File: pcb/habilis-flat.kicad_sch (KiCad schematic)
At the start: 74 parts, among them SW1 MX, SW10 MX, SW11 MX, SW12 MX, SW13 MX, SW14 MX, SW15 MX, SW16 MX, SW17 MX, SW18 MX, SW19 MX, SW2 MX, SW20 MX, SW21 MX, SW22 MX, SW23 MX, SW24 MX, SW25 MX, SW26 MX, SW27 MX, SW28 MX, SW29 MX, SW3 MX, SW30 MX, SW31 MX, SW32 MX, SW33 MX, SW34 MX, SW35 MX, SW4 MX, SW5 MX, SW6 MX, SW7 MX, SW8 MX, SW9 MX, U1 ProMicro

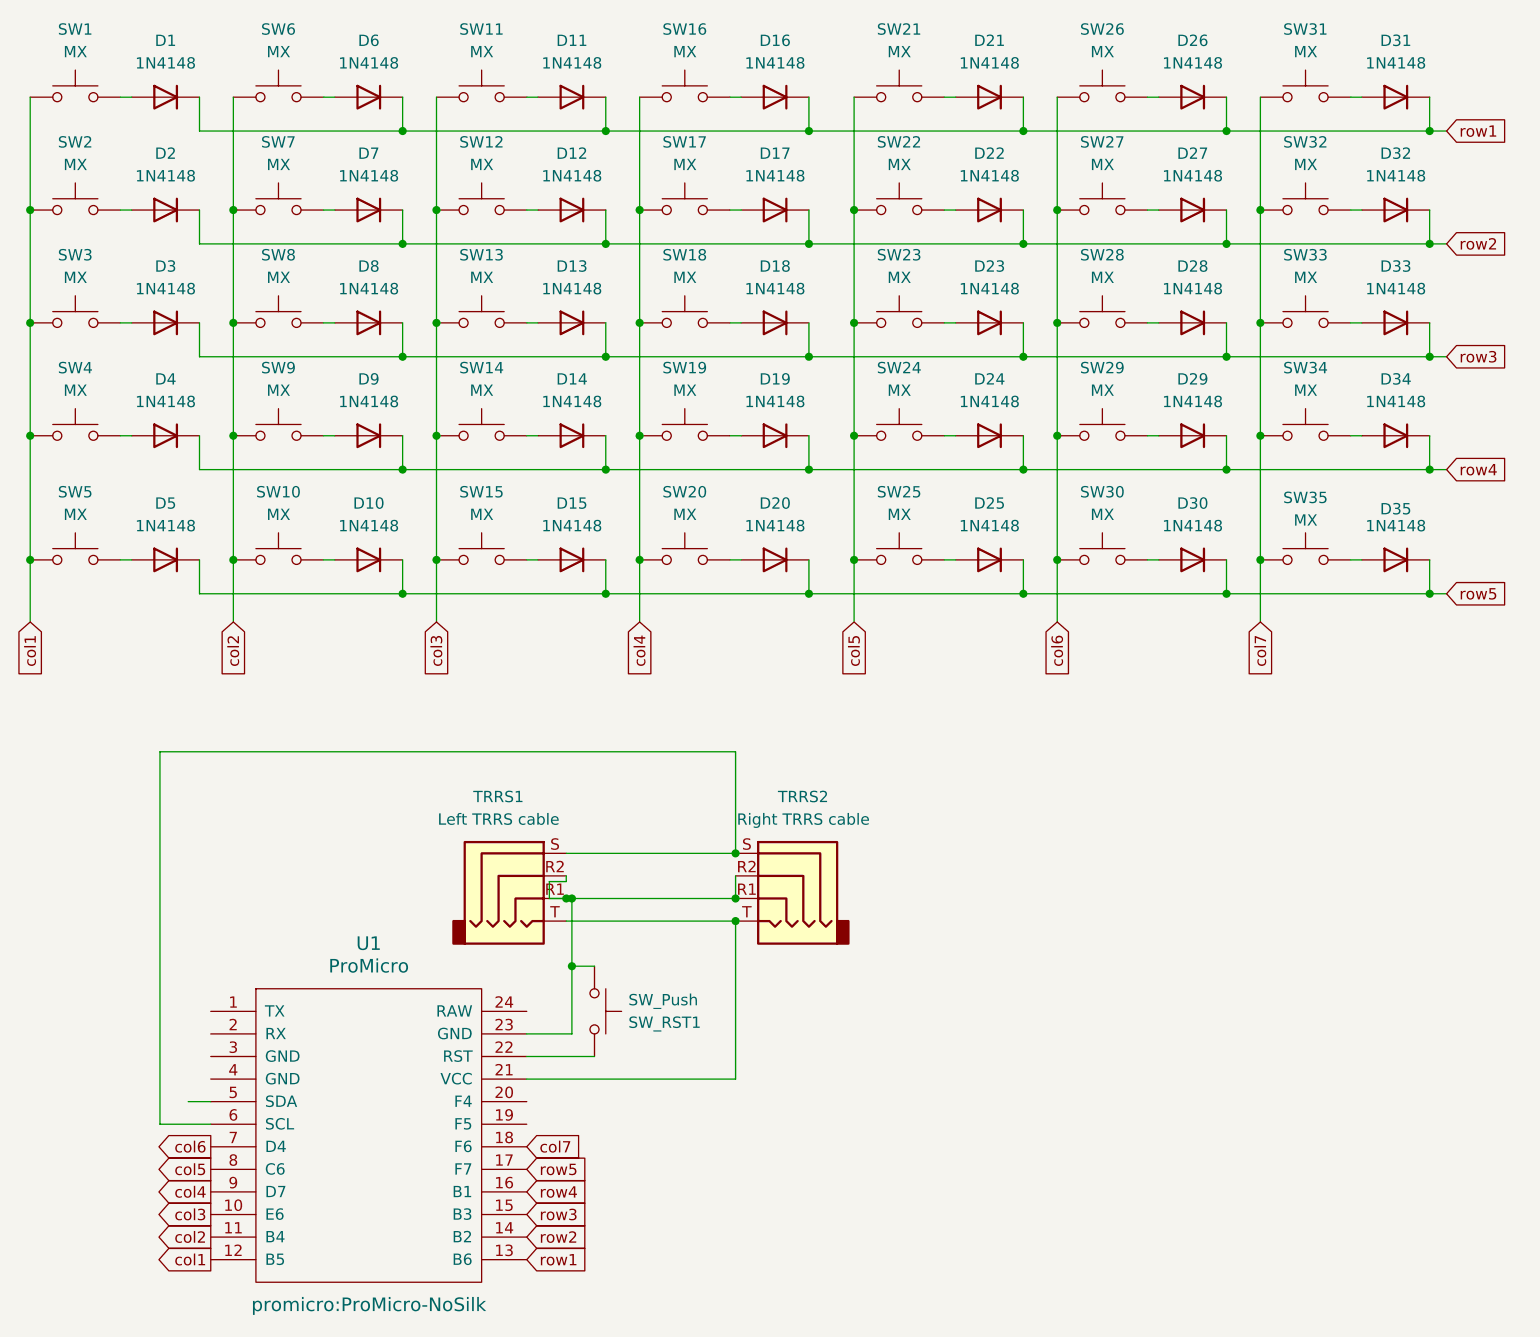
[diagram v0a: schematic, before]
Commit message: Renumber rows and columns to start at 0
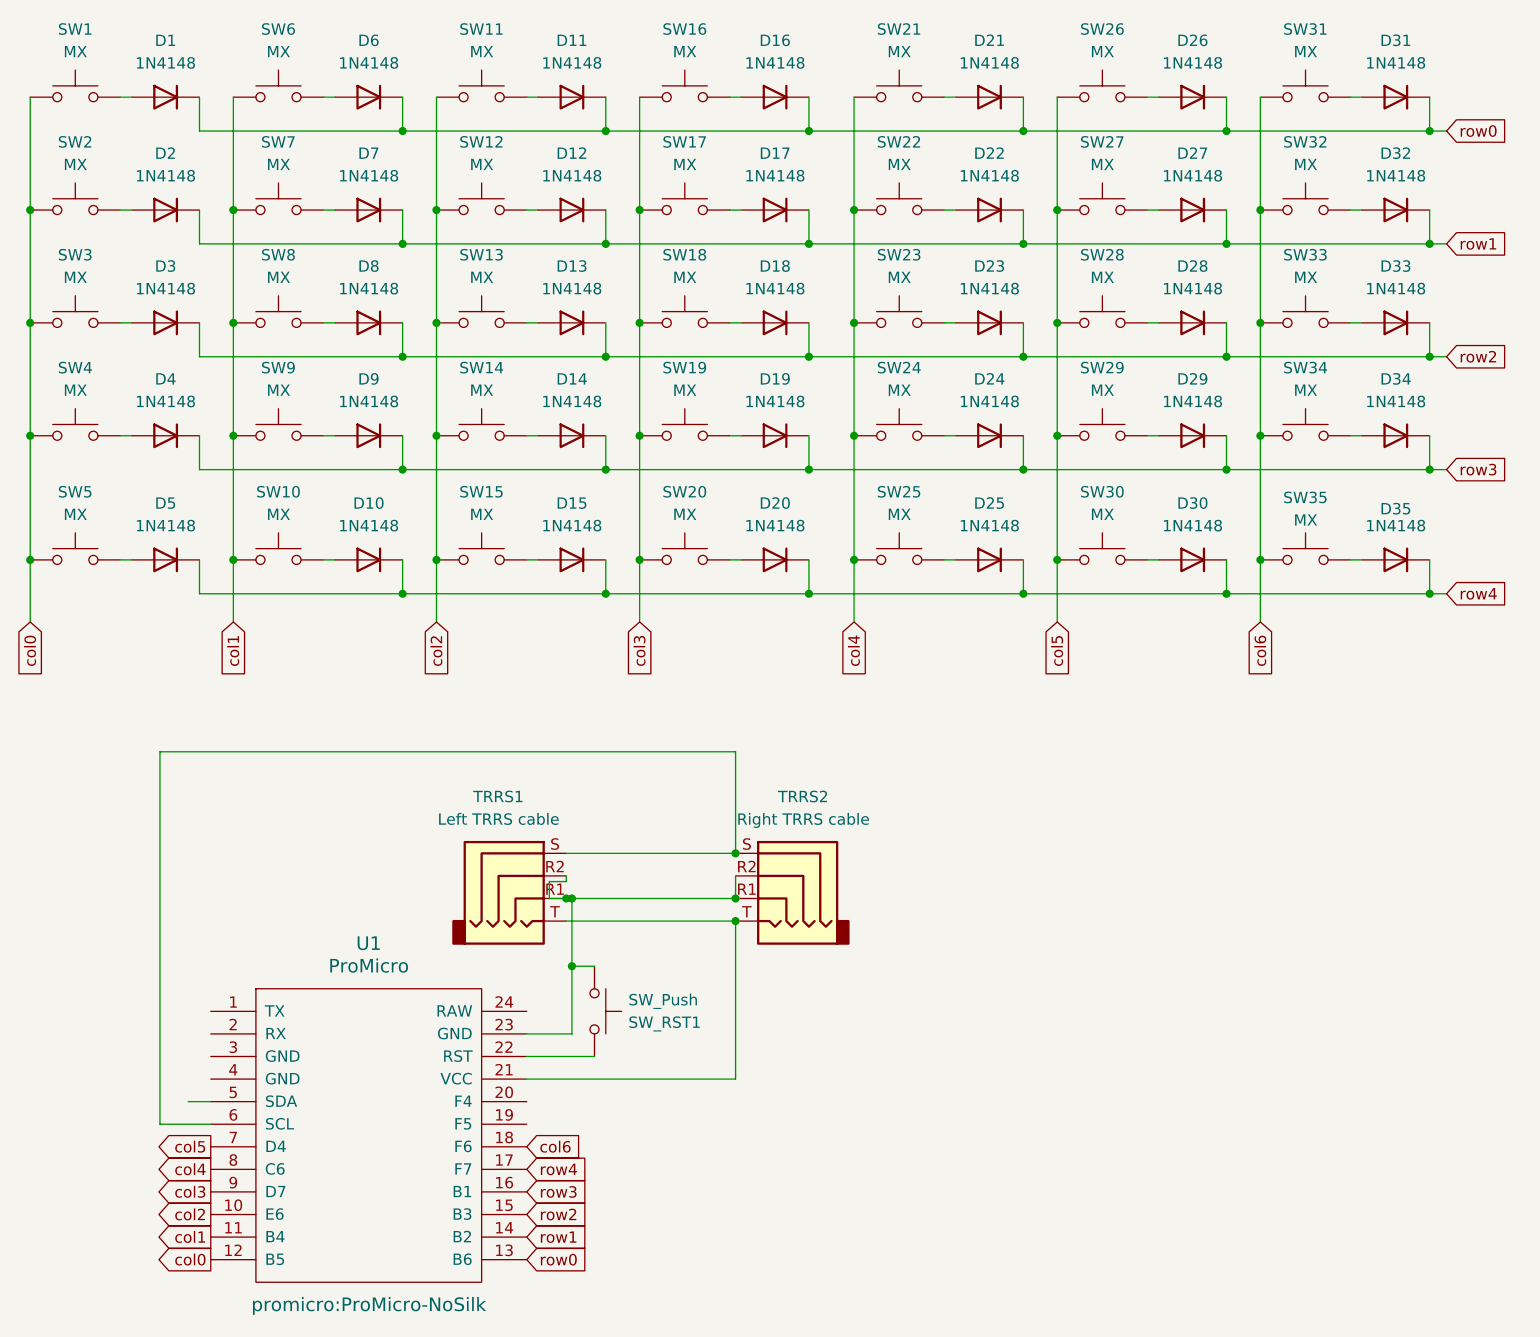
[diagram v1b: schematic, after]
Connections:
- net col7 is gone; now on net col6: SW31.2, SW32.2, SW33.1, SW34.2, SW35.2, U1.18 (F6)
- net row5 is gone; now on net row4: D10.1 (K), D15.1 (K), D20.1 (K), D25.1 (K), D30.1 (K), D35.1 (K), D5.1 (K), U1.17 (F7)
- net col1: now also SW10.2, SW6.2, SW7.2, SW8.2, SW9.2, U1.11 (B4); no longer SW1.2, SW2.2, SW3.2, SW4.2, SW5.2, U1.12 (B5)
- net col2: now also SW11.2, SW12.2, SW13.2, SW14.2, SW15.2, U1.10 (E6); no longer SW10.2, SW6.2, SW7.2, SW8.2, SW9.2, U1.11 (B4)
- net col3: now also SW16.2, SW17.2, SW18.2, SW19.2, SW20.2, U1.9 (D7); no longer SW11.2, SW12.2, SW13.2, SW14.2, SW15.2, U1.10 (E6)
- net col4: now also SW21.2, SW22.2, SW23.2, SW24.2, SW25.2, U1.8 (C6); no longer SW16.2, SW17.2, SW18.2, SW19.2, SW20.2, U1.9 (D7)
- net col5: now also SW26.2, SW27.2, SW28.2, SW29.2, SW30.2, U1.7 (D4); no longer SW21.2, SW22.2, SW23.2, SW24.2, SW25.2, U1.8 (C6)
- net col6: no longer SW26.2, SW27.2, SW28.2, SW29.2, SW30.2, U1.7 (D4)
- net row1: now also D12.1 (K), D17.1 (K), D2.1 (K), D22.1 (K), D27.1 (K), D32.1 (K), D7.1 (K), U1.14 (B2); no longer D1.1 (K), D11.1 (K), D16.1 (K), D21.1 (K), D26.1 (K), D31.1 (K), D6.1 (K), U1.13 (B6)
- net row2: now also D13.1 (K), D18.1 (K), D23.1 (K), D28.1 (K), D3.1 (K), D33.1 (K), D8.1 (K), U1.15 (B3); no longer D12.1 (K), D17.1 (K), D2.1 (K), D22.1 (K), D27.1 (K), D32.1 (K), D7.1 (K), U1.14 (B2)
- net row3: now also D14.1 (K), D19.1 (K), D24.1 (K), D29.1 (K), D34.1 (K), D4.1 (K), D9.1 (K), U1.16 (B1); no longer D13.1 (K), D18.1 (K), D23.1 (K), D28.1 (K), D3.1 (K), D33.1 (K), D8.1 (K), U1.15 (B3)
- net row4: no longer D14.1 (K), D19.1 (K), D24.1 (K), D29.1 (K), D34.1 (K), D4.1 (K), D9.1 (K), U1.16 (B1)
- new net col0: SW1.2, SW2.2, SW3.2, SW4.2, SW5.2, U1.12 (B5)
- new net row0: D1.1 (K), D11.1 (K), D16.1 (K), D21.1 (K), D26.1 (K), D31.1 (K), D6.1 (K), U1.13 (B6)
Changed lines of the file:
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@@
     (stroke (width 0) (type default))
   )
-  (global_label "row4" (shape input) (at 194.945 74.93 0) (fields_autoplaced)
+  (global_label "row3" (shape input) (at 194.945 74.93 0) (fields_autoplaced)
     (effects (font (size 1.27 1.27)) (justify left))
     (property "Intersheetrefs" "${INTERSHEET_REFS}" (at 202.4054 74.93 0)
@@
     )
   )
-  (global_label "row1" (shape input) (at 91.44 163.83 0) (fields_autoplaced)
+  (global_label "row0" (shape input) (at 91.44 163.83 0) (fields_autoplaced)
     (effects (font (size 1.27 1.27)) (justify left))
     (property "Intersheetrefs" "${INTERSHEET_REFS}" (at 98.9004 163.83 0)
@@
     )
   )
-  (global_label "col2" (shape input) (at 58.42 92.075 270) (fields_autoplaced)
+  (global_label "col1" (shape input) (at 58.42 92.075 270) (fields_autoplaced)
     (effects (font (size 1.27 1.27)) (justify right))
     (property "Intersheetrefs" "${INTERSHEET_REFS}" (at 58.42 99.1725 90)
@@
     )
   )
-  (global_label "row3" (shape input) (at 91.44 158.75 0) (fields_autoplaced)
+  (global_label "row2" (shape input) (at 91.44 158.75 0) (fields_autoplaced)
     (effects (font (size 1.27 1.27)) (justify left))
     (property "Intersheetrefs" "${INTERSHEET_REFS}" (at 98.9004 158.75 0)
@@
     )
   )
-  (global_label "col2" (shape output) (at 55.88 161.29 180) (fields_autoplaced)
+  (global_label "col1" (shape output) (at 55.88 161.29 180) (fields_autoplaced)
     (effects (font (size 1.27 1.27)) (justify right))
     (property "Intersheetrefs" "${INTERSHEET_REFS}" (at 48.7825 161.29 0)
@@
     )
   )
-  (global_label "col3" (shape output) (at 55.88 158.75 180) (fields_autoplaced)
+  (global_label "col2" (shape output) (at 55.88 158.75 180) (fields_autoplaced)
     (effects (font (size 1.27 1.27)) (justify right))
     (property "Intersheetrefs" "${INTERSHEET_REFS}" (at 48.7825 158.75 0)
@@
     )
   )
-  (global_label "row5" (shape input) (at 91.44 153.67 0) (fields_autoplaced)
+  (global_label "row4" (shape input) (at 91.44 153.67 0) (fields_autoplaced)
     (effects (font (size 1.27 1.27)) (justify left))
     (property "Intersheetrefs" "${INTERSHEET_REFS}" (at 98.9004 153.67 0)
@@
     )
   )
-  (global_label "col6" (shape input) (at 151.13 92.075 270) (fields_autoplaced)
+  (global_label "col5" (shape input) (at 151.13 92.075 270) (fields_autoplaced)
     (effects (font (size 1.27 1.27)) (justify right))
     (property "Intersheetrefs" "${INTERSHEET_REFS}" (at 151.13 99.1725 90)
@@
     )
   )
-  (global_label "col4" (shape output) (at 55.88 156.21 180) (fields_autoplaced)
+  (global_label "col3" (shape output) (at 55.88 156.21 180) (fields_autoplaced)
     (effects (font (size 1.27 1.27)) (justify right))
     (property "Intersheetrefs" "${INTERSHEET_REFS}" (at 48.7825 156.21 0)
@@
     )
   )
-  (global_label "col1" (shape output) (at 55.88 163.83 180) (fields_autoplaced)
+  (global_label "col0" (shape output) (at 55.88 163.83 180) (fields_autoplaced)
     (effects (font (size 1.27 1.27)) (justify right))
     (property "Intersheetrefs" "${INTERSHEET_REFS}" (at 48.7825 163.83 0)
@@
     )
   )
-  (global_label "col3" (shape input) (at 81.28 92.075 270) (fields_autoplaced)
+  (global_label "col2" (shape input) (at 81.28 92.075 270) (fields_autoplaced)
     (effects (font (size 1.27 1.27)) (justify right))
     (property "Intersheetrefs" "${INTERSHEET_REFS}" (at 81.28 99.1725 90)
@@
     )
   )
-  (global_label "row3" (shape input) (at 194.945 62.23 0) (fields_autoplaced)
+  (global_label "row2" (shape input) (at 194.945 62.23 0) (fields_autoplaced)
     (effects (font (size 1.27 1.27)) (justify left))
     (property "Intersheetrefs" "${INTERSHEET_REFS}" (at 202.4054 62.23 0)
@@
     )
   )
-  (global_label "row4" (shape input) (at 91.44 156.21 0) (fields_autoplaced)
+  (global_label "row3" (shape input) (at 91.44 156.21 0) (fields_autoplaced)
     (effects (font (size 1.27 1.27)) (justify left))
     (property "Intersheetrefs" "${INTERSHEET_REFS}" (at 98.9004 156.21 0)
@@
     )
   )
-  (global_label "col7" (shape input) (at 91.44 151.13 0) (fields_autoplaced)
+  (global_label "col6" (shape input) (at 91.44 151.13 0) (fields_autoplaced)
     (effects (font (size 1.27 1.27)) (justify left))
     (property "Intersheetrefs" "${INTERSHEET_REFS}" (at 98.5375 151.13 0)
@@
     )
   )
-  (global_label "col7" (shape input) (at 173.99 92.075 270) (fields_autoplaced)
+  (global_label "col6" (shape input) (at 173.99 92.075 270) (fields_autoplaced)
     (effects (font (size 1.27 1.27)) (justify right))
     (property "Intersheetrefs" "${INTERSHEET_REFS}" (at 173.99 99.1725 90)
@@
     )
   )
-  (global_label "row1" (shape input) (at 194.945 36.83 0) (fields_autoplaced)
+  (global_label "row0" (shape input) (at 194.945 36.83 0) (fields_autoplaced)
     (effects (font (size 1.27 1.27)) (justify left))
     (property "Intersheetrefs" "${INTERSHEET_REFS}" (at 202.4054 36.83 0)
@@
     )
   )
-  (global_label "row2" (shape input) (at 91.44 161.29 0) (fields_autoplaced)
+  (global_label "row1" (shape input) (at 91.44 161.29 0) (fields_autoplaced)
     (effects (font (size 1.27 1.27)) (justify left))
     (property "Intersheetrefs" "${INTERSHEET_REFS}" (at 98.9004 161.29 0)
@@
     )
   )
-  (global_label "col5" (shape input) (at 128.27 92.075 270) (fields_autoplaced)
+  (global_label "col4" (shape input) (at 128.27 92.075 270) (fields_autoplaced)
     (effects (font (size 1.27 1.27)) (justify right))
     (property "Intersheetrefs" "${INTERSHEET_REFS}" (at 128.27 99.1725 90)
@@
     )
   )
-  (global_label "col1" (shape input) (at 35.56 92.075 270) (fields_autoplaced)
+  (global_label "col0" (shape input) (at 35.56 92.075 270) (fields_autoplaced)
     (effects (font (size 1.27 1.27)) (justify right))
     (property "Intersheetrefs" "${INTERSHEET_REFS}" (at 35.56 99.1725 90)
@@
     )
   )
-  (global_label "row5" (shape input) (at 194.945 88.9 0) (fields_autoplaced)
+  (global_label "row4" (shape input) (at 194.945 88.9 0) (fields_autoplaced)
     (effects (font (size 1.27 1.27)) (justify left))
     (property "Intersheetrefs" "${INTERSHEET_REFS}" (at 202.4054 88.9 0)
@@
     )
   )
-  (global_label "col5" (shape output) (at 55.88 153.67 180) (fields_autoplaced)
+  (global_label "col4" (shape output) (at 55.88 153.67 180) (fields_autoplaced)
     (effects (font (size 1.27 1.27)) (justify right))
     (property "Intersheetrefs" "${INTERSHEET_REFS}" (at 48.7825 153.67 0)
@@
     )
   )
-  (global_label "col6" (shape output) (at 55.88 151.13 180) (fields_autoplaced)
+  (global_label "col5" (shape output) (at 55.88 151.13 180) (fields_autoplaced)
     (effects (font (size 1.27 1.27)) (justify right))
     (property "Intersheetrefs" "${INTERSHEET_REFS}" (at 48.7825 151.13 0)
@@
     )
   )
-  (global_label "row2" (shape input) (at 194.945 49.53 0) (fields_autoplaced)
+  (global_label "row1" (shape input) (at 194.945 49.53 0) (fields_autoplaced)
     (effects (font (size 1.27 1.27)) (justify left))
     (property "Intersheetrefs" "${INTERSHEET_REFS}" (at 202.4054 49.53 0)
@@
     )
   )
-  (global_label "col4" (shape input) (at 104.14 92.075 270) (fields_autoplaced)
+  (global_label "col3" (shape input) (at 104.14 92.075 270) (fields_autoplaced)
     (effects (font (size 1.27 1.27)) (justify right))
     (property "Intersheetrefs" "${INTERSHEET_REFS}" (at 104.14 99.1725 90)

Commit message: Simplify schematic, pacify ERC
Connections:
- net GND: now reaches SW_RST1.2, TRRS1.R1, TRRS1.R2, TRRS2.R1, TRRS2.R2, U1.23 (GND)
- no-connect marks 0 -> 8
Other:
- moved on the sheet: SW_RST1

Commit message: Replace reset button fp with one I have at hand
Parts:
- SW_RST1: footprint Button_Switch_THT:SW_PUSH_6mm -> project-components:that_push_button_i_have_in_stock
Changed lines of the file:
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@@
       (effects (font (size 1.27 1.27)) (justify left))
     )
-    (property "Footprint" "Button_Switch_THT:SW_PUSH_6mm" (at 106.045 135.89 0)
+    (property "Footprint" "project-components:that_push_button_i_have_in_stock" (at 106.045 135.89 0)
       (effects (font (size 1.27 1.27)) hide)
     )
